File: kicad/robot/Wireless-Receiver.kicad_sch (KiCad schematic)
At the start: 49 parts, among them IC2 STWLC38JRM, J8 Conn_01x02

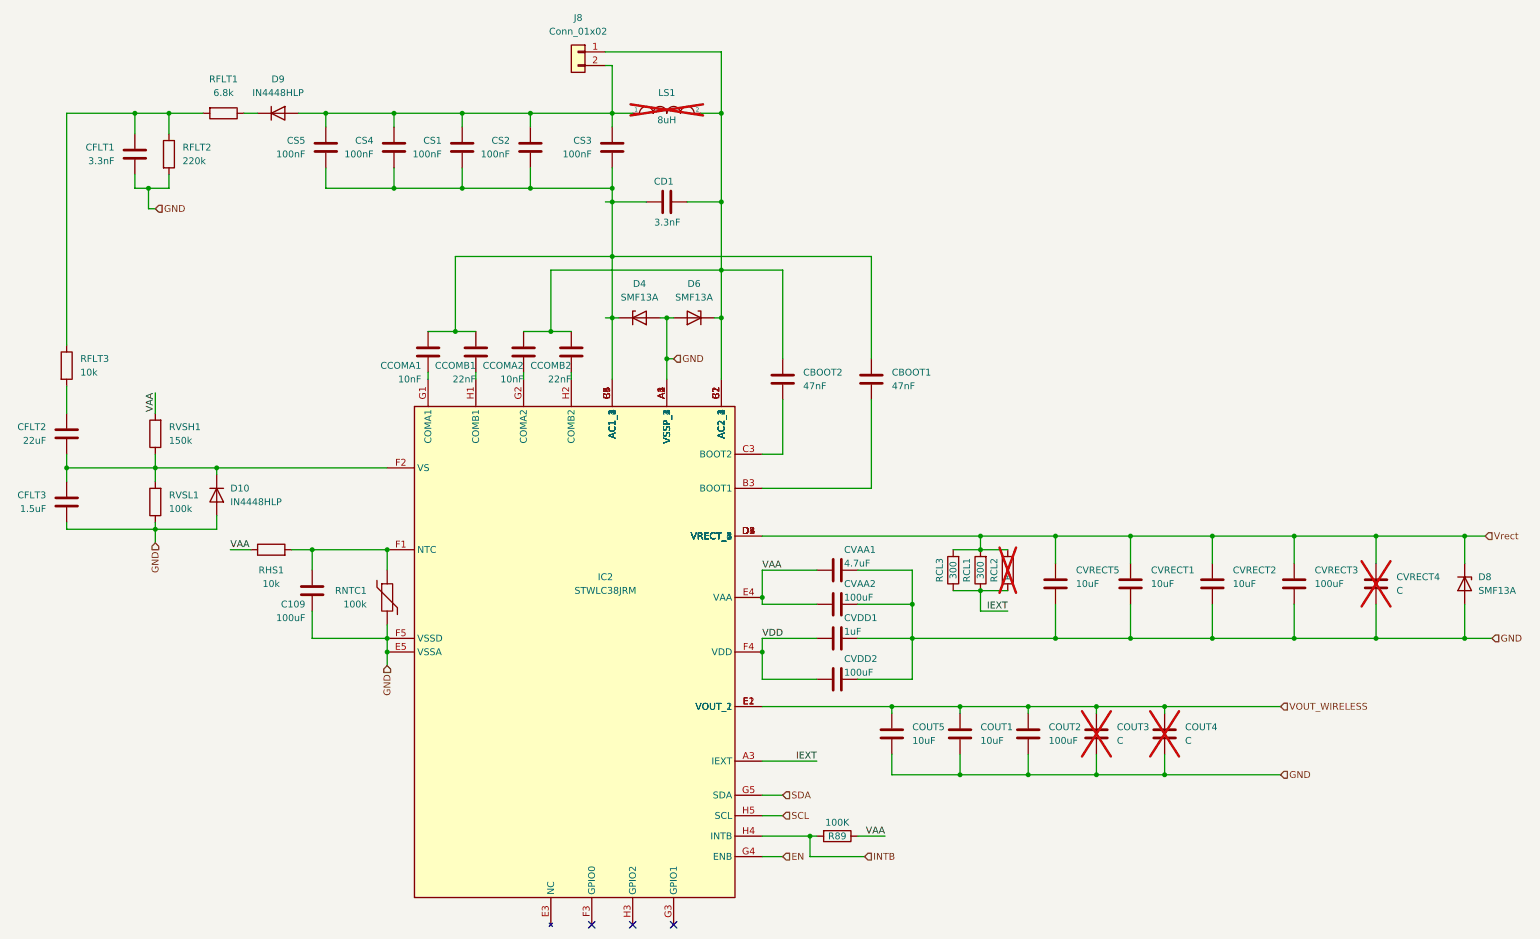
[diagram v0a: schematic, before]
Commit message: Changed 4.7uF caps to 0603 and update ref names for wireless sheet as caused BOM issues
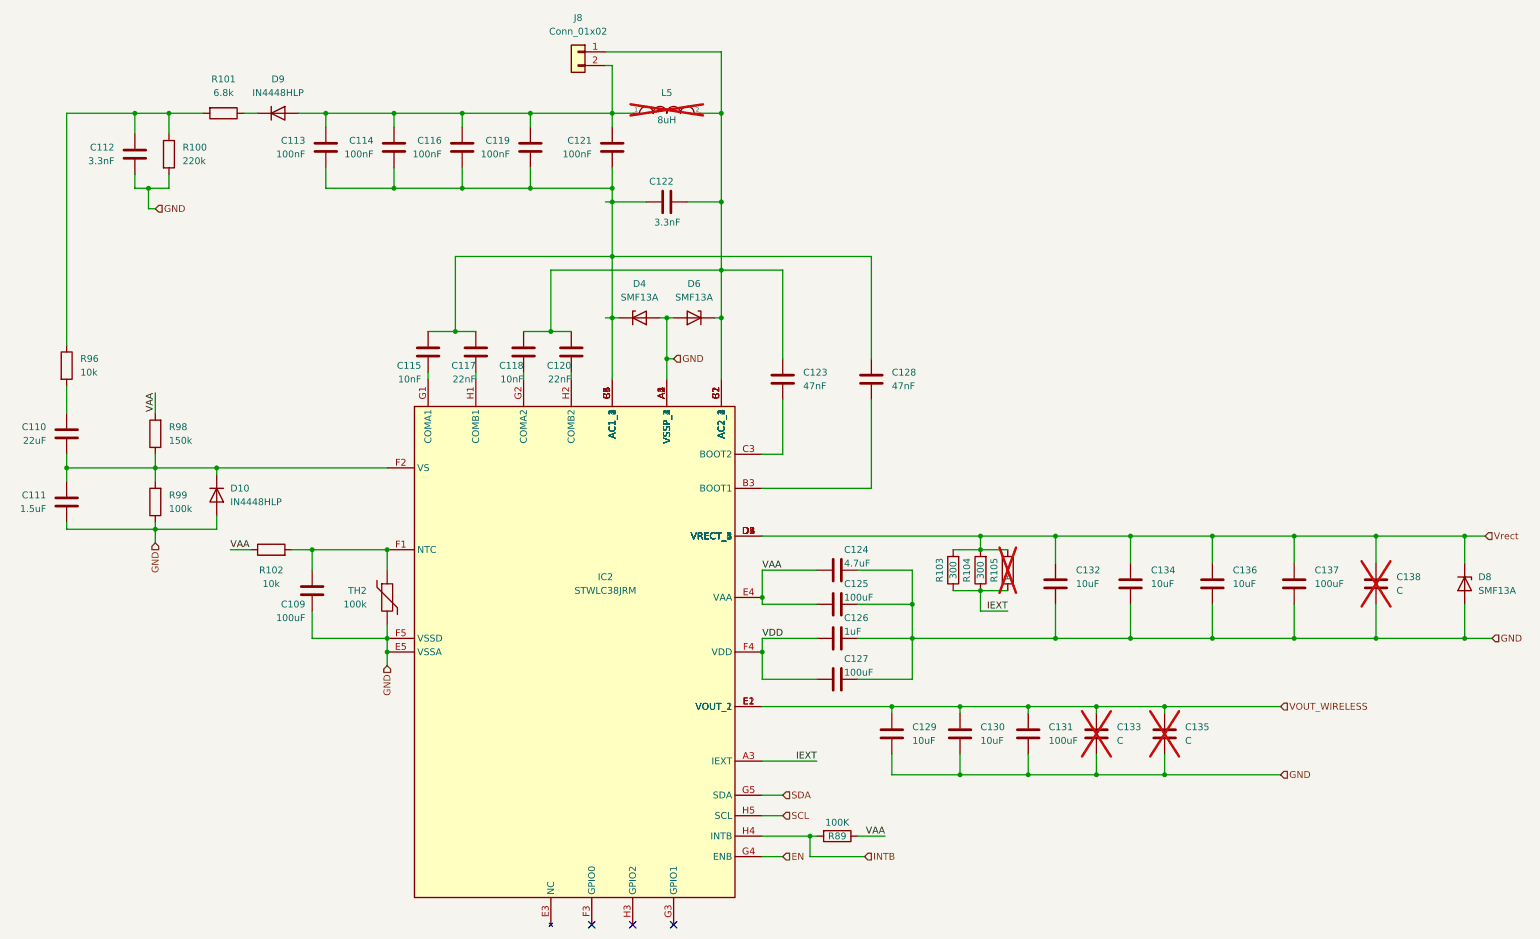
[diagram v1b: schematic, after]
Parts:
- C109: Manufacturer (none) -> Murata; Part Number (none) -> GRM21BR60E107ME15K
- C125: renamed from CVAA2; Manufacturer (none) -> Murata; Part Number (none) -> GRM21BR60E107ME15K
- C127: renamed from CVDD2; Manufacturer (none) -> Murata; Part Number (none) -> GRM21BR60E107ME15K
- C131: renamed from COUT2; Manufacturer (none) -> Murata; Part Number (none) -> GRM21BR60E107ME15K
- C137: renamed from CVRECT3; Manufacturer (none) -> Murata; Part Number (none) -> GRM21BR60E107ME15K
- IC2: Arrow Part Number STWLC38JRM -> (none); Arrow Price/Stock https://www.arrow.com/en/products/stwlc38jrm/stmicroelectro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 -> (none); Height 0.567 -> (none); Manufacturer (none) -> STMicroelectronics; Manufacturer_Name STMicroelectronics -> (none); Manufacturer_Part_Number STWLC38JRM -> (none); Mouser Part Number 511-STWLC38JRM -> (none); Mouser Price/Stock https://www.mouser.co.uk/ProductDetail/STMicroelectronics/S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 -> (none); Part Number (none) -> STWLC38JRM
- renumbered CFLT2 to C110, CFLT3 to C111, CFLT1 to C112, CS5 to C113, CS4 to C114, CCOMA1 to C115, CS1 to C116, CCOMB1 to C117, CCOMA2 to C118, CS2 to C119, CCOMB2 to C120, CS3 to C121, CD1 to C122, CBOOT2 to C123, CVAA1 to C124, CVDD1 to C126, CBOOT1 to C128, COUT5 to C129, COUT1 to C130, CVRECT5 to C132, COUT3 to C133, CVRECT1 to C134, COUT4 to C135, CVRECT2 to C136, CVRECT4 to C138, LS1 to L5, RFLT2 to R100, RFLT1 to R101, RHS1 to R102, RCL3 to R103, RCL1 to R104, RCL2 to R105, RFLT3 to R96, RVSH1 to R98, RVSL1 to R99, RNTC1 to TH2

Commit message: Updating all wireless passives to required part numbers. Still missing less restrictive ones
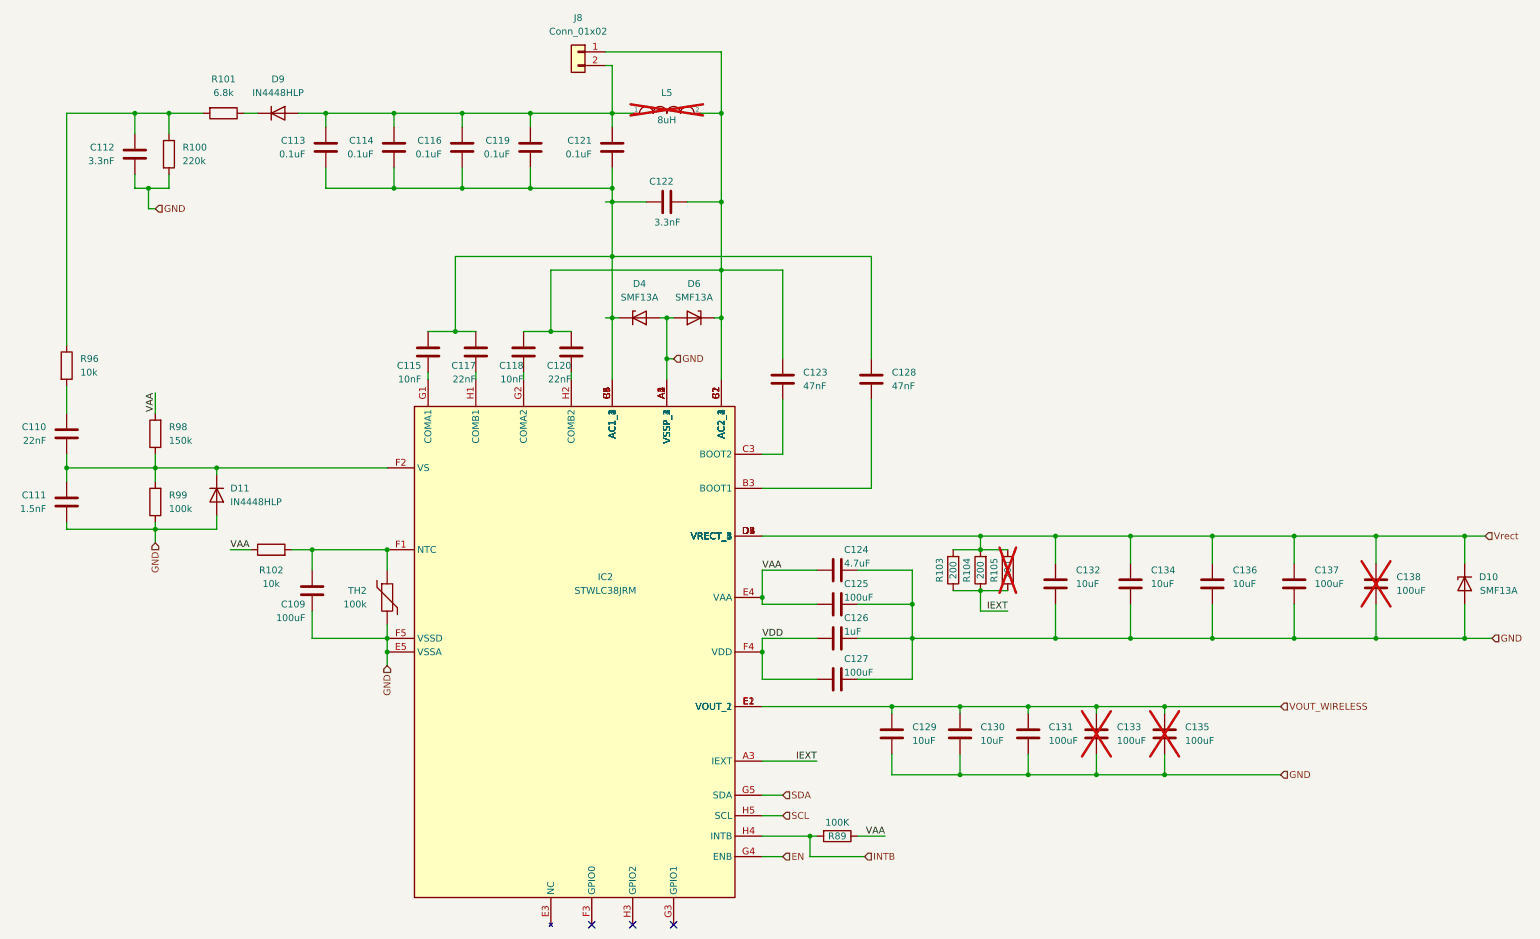
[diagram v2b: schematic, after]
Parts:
- removed D10: IN4448HLP, symbol Device:D
- removed D8: SMF13A, symbol Device:D_Zener
- added D10: SMF13A, robot:D_SOD-123F, symbol Device:D_Zener
- added D11: IN4448HLP, robot:D_0402_1005Metric, symbol Device:D
- C110: value 22uF -> 22nF; footprint robot:C_0603_1608Metric -> robot:C_0402_1005Metric; Manufacturer (none) -> Murata; Part Number (none) -> GRM155R71H223KA12J; V_Max (none) -> 50V
- C111: value 1.5uF -> 1.5nF; Manufacturer (none) -> Murata; Part Number (none) -> GCM155R71H152KA37D; V_Max (none) -> 50V
- C112: footprint robot:C_0603_1608Metric -> robot:C_0402_1005Metric; Manufacturer (none) -> Murata; Part Number (none) -> GCM155R71H332KA37J; V_Max (none) -> 50V
- C113, C114, C116, C119, C121: value 100nF -> 0.1uF; footprint robot:C_0603_1608Metric -> robot:C_0402_1005Metric; Manufacturer (none) -> Murata; Part Number (none) -> GRM155R62A104KE14D
- C115, C117, C118, C120, C123, C126, C128: footprint robot:C_0603_1608Metric -> robot:C_0402_1005Metric
- C122: footprint robot:C_0603_1608Metric -> robot:C_0402_1005Metric; Manufacturer (none) -> Murata; Part Number (none) -> GCM155R71H332KA37J
- C124: Manufacturer (none) -> Samsung; Part Number (none) -> CL10A475KQ8NNNC
- C129, C130, C132, C134, C136: Manufacturer (none) -> Murata; Part Number (none) -> GRM188R61E106KA73J
- C133, C135, C138: value C -> 100uF; footprint robot:C_0603_1608Metric -> robot:C_0805_2012Metric
- D4, D6: footprint (none) -> robot:D_SOD-123F; Manufacturer (none) -> Littelfuse Inc.; Part Number (none) -> SMF13A
- D9: footprint (none) -> robot:D_0402_1005Metric; Manufacturer (none) -> Diodes Incorporated; Part Number (none) -> 1N4448HLP-7
- R100: footprint robot:R_0603_1608Metric -> robot:R_0402_1005Metric
- R103, R104: value 300 -> 200; Manufacturer (none) -> Panasonic; Notes (none) -> Requires Pulse Withstanding; Part Number (none) -> ERJ-PA3J201V
- R105: value R -> 200; Manufacturer (none) -> Panasonic; Notes (none) -> Requires Pulse Withstanding; Part Number (none) -> ERJ-PA3J201V
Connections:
- net GND: now also D10.2 (A), D11.2 (A)
- net Vrect: now also D10.1 (K)
- net at C110.1, C111.2, IC2.F2 (VS)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: now also D11.1 (K)

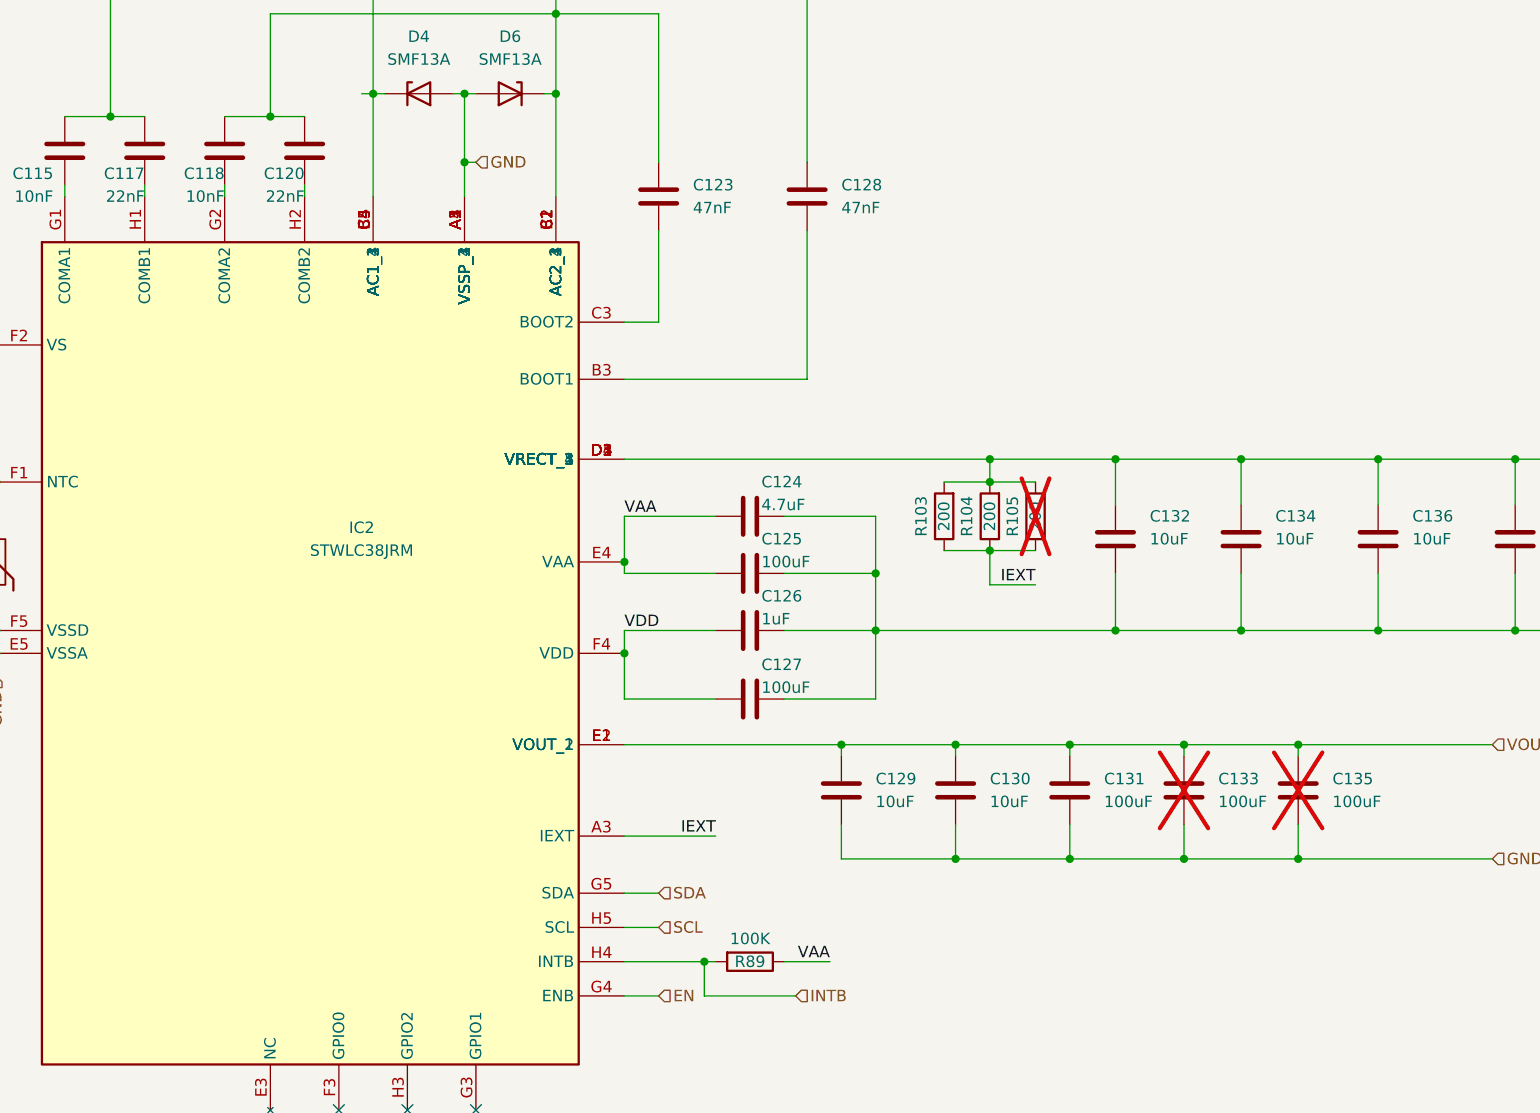
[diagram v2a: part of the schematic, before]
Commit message: All BOM and footprints other than 100uF selected
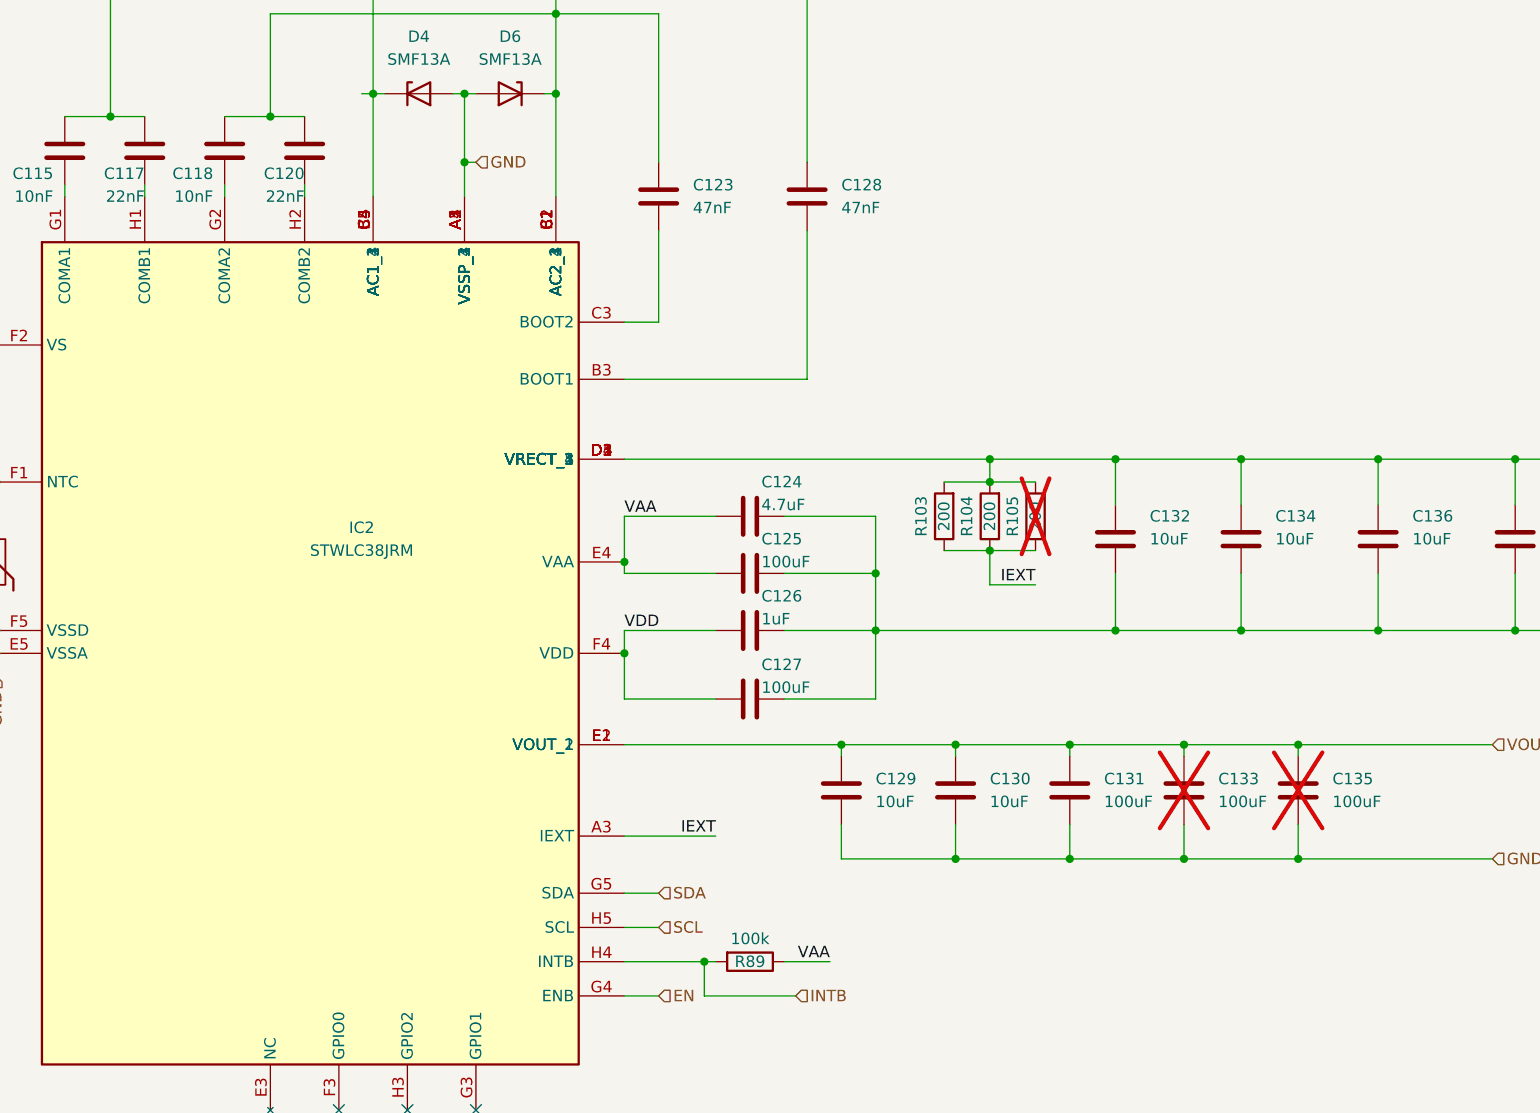
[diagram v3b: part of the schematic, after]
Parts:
- C109, C125, C127, C131, C137: Part Number GRM21BR60E107ME15K -> (none)
- C115, C118: Manufacturer (none) -> Würth Elektronik; Part Number (none) -> 885012205067
- C117, C120: Manufacturer (none) -> Murata; Part Number (none) -> GRM155R71H223KA12J
- C123, C128: Manufacturer (none) -> Murata; Part Number (none) -> GRM155R71H473KE14D
- C124: Manufacturer Samsung -> Murata; Part Number CL10A475KQ8NNNC -> GRM188R61E475KE11D
- C126: Manufacturer (none) -> Murata; Part Number (none) -> GRM155R61E105KA12D
- C133, C135, C138: Manufacturer (none) -> Murata
- J8: footprint robot:THT_Pitch2.54mm_Drill1.0mm -> robot:THT_Pitch5mm_Drill1.2mm; Manufacturer (none) -> N/A; Part Number (none) -> N/A
- L5: Manufacturer (none) -> Würth Elektronik; Part Number (none) -> 760308102207
- R100: Manufacturer (none) -> YAGEO; Part Number (none) -> RC0402FR-07220KL
- R101: Manufacturer (none) -> YAGEO; Part Number (none) -> RC0402FR-136K8L
- R102, R96: Manufacturer (none) -> Walsin Technology; Part Number (none) -> WR06X1002FTL
- R89: value 100K -> 100k; Manufacturer (none) -> Walsin Technology; Part Number (none) -> WR06X1003FTL
- R98: footprint robot:R_0603_1608Metric -> robot:R_0402_1005Metric; Manufacturer (none) -> YAGEO; Part Number (none) -> RC0402FR-13150KL
- R99: Manufacturer (none) -> Walsin Technology; Part Number (none) -> WR06X1003FTL
- TH2: footprint (none) -> robot:R_0402_1005Metric; Manufacturer (none) -> Murata; Part Number (none) -> NCU15WF104J6SRC
